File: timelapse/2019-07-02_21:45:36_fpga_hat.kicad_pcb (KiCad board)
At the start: 4 copper layers, 65 x 56.5 mm, 90 parts, among them J1 2x20, J2 AudioJack3, J3 Conn_02x06_Top_Bottom, J4 Conn_02x06_Top_Bottom, J5 Conn_02x06_Top_Bottom, J6 Conn_01x02, SW1 PTS815, SW2 PTS815, SW3 PTS815, SW4 PTS815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

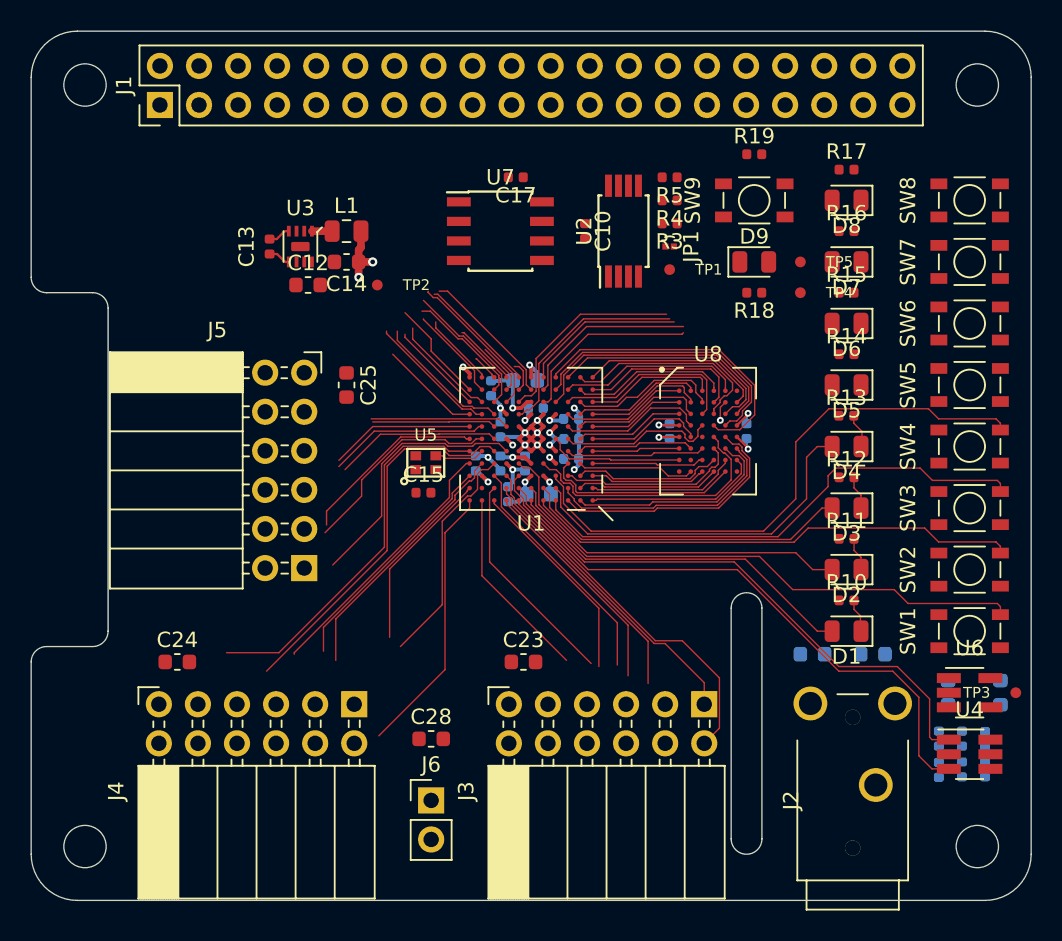
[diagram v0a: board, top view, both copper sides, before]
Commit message: Continue BGA route-out. SRAM connected, start heading out toward LEDs and IO.
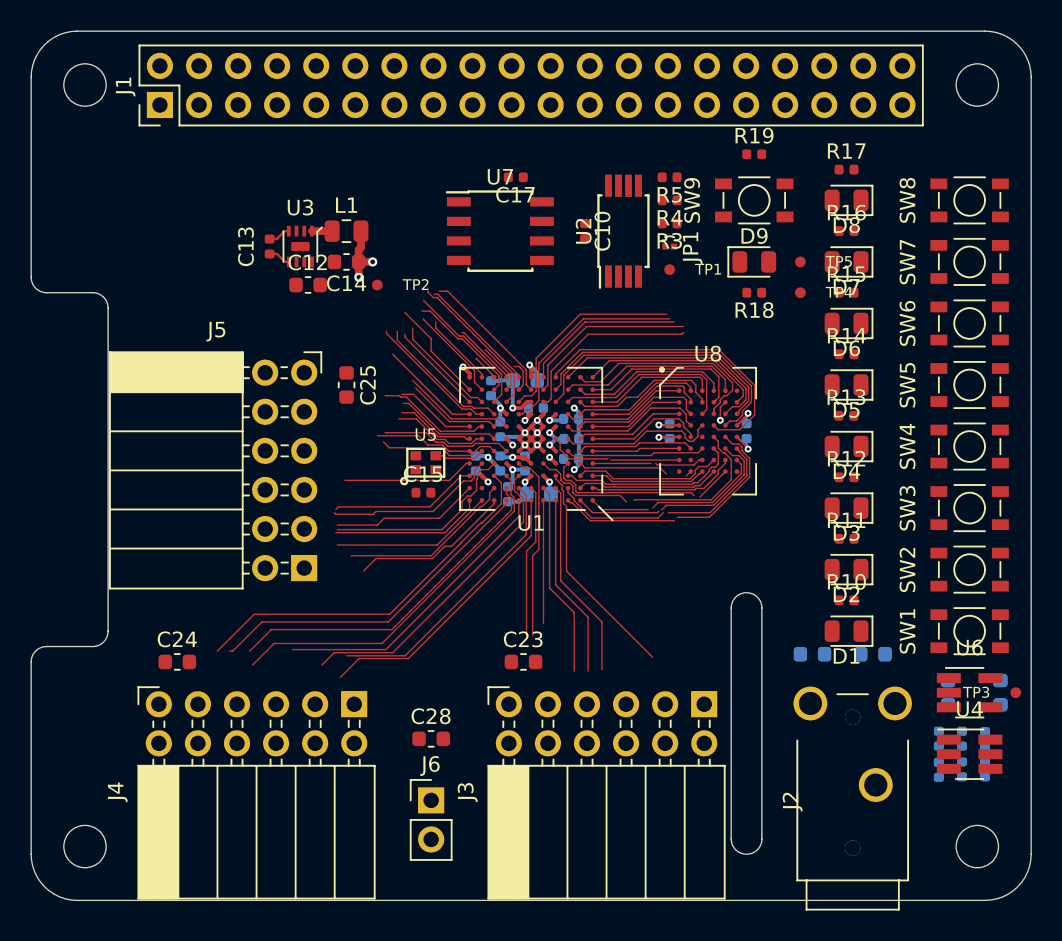
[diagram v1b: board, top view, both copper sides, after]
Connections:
- U1 pad A1: /SRAM_DQ7 -> /IO2_4
- U1 pad A11: /IO0_6 -> /IO0_0
- U1 pad A2: /SRAM_DQ5 -> /IO2_2
- U1 pad A3: /SRAM_DQ4 -> /IO2_3
- U1 pad A4: /SW2 -> /IO1_6
- U1 pad A5: /SW1 -> /IO1_4
- U1 pad A6: /LED0 -> /IO1_3
- U1 pad A7: /IO0_4 -> /IO1_2
- U1 pad B3: /SRAM_DQ6 -> /IO2_1
- U1 pad B4: /LED3 -> /IO2_0
- U1 pad B5: /LED2 -> /IO1_5
- U1 pad B6: /SW0 -> /IO2_6
- U1 pad B7: /AUDIO_L_PWM -> /IO2_5
- U1 pad B8: /IO1_2 -> /IO0_4
- U1 pad C4: /SW3 -> /SRAM_A11
- U1 pad C7: /AUDIO_R_PWM -> /IO1_1
- U1 pad C8: /IO0_0 -> /IO0_6
- U1 pad D2: /SRAM_A8 -> /SRAM_DQ15
- U1 pad D3: /SRAM_A11 -> /SRAM_A8
- U1 pad D5: /SRAM_A16 -> /IO1_7
- U1 pad D7: /LED1 -> /IO0_7
- U1 pad E8: /IO2_1 -> /SW3
- U1 pad E9: /IO1_6 -> /SW2
- U1 pad F10: /IO2_6 -> /SW0
- U1 pad F11: /IO2_5 -> /AUDIO_L_PWM
- U1 pad F4: /SRAM_DQ15 -> /SRAM_DQ6
- U1 pad F9: /IO1_4 -> /SW1
- U1 pad G8: /IO2_0 -> /LED3
- U1 pad H10: /IO0_7 -> /LED1
- U1 pad H7: /IO2_4 -> /SRAM_DQ7
- U1 pad J10: /IO1_5 -> /LED2
- U1 pad J5: /IO2_2 -> /SRAM_DQ5
- U1 pad J7: /IO2_3 -> /SRAM_DQ4
- U1 pad J8: /GP27_SDIO_DAT3 -> /GP22_SDIO_CLK
- U1 pad K11: /IO1_3 -> /LED0
- U1 pad K5: /IO1_7 -> /SRAM_A16
- U1 pad K6: /GP22_SDIO_CLK -> /GP27_SDIO_DAT3
- U1 pad K7: /IO1_1 -> /AUDIO_R_PWM
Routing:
- net /AUDIO_R_PWM: track 39.3 -> 2.04 mm
- net /AUDIO_L_PWM: track 36.5 -> 5.10 mm
- net /SW3: track 37.4 -> 8.55 mm
- net /SW0: track 34.7 -> 6.19 mm
- net /SW2: track 33.4 -> 7.96 mm
- net /SW1: track 32.3 -> 6.85 mm
- net /IO1_1: track 2.04 -> 20.4 mm
- net /SW5: track 24.6 -> 6.41 mm
- net /LED0: track 23.3 -> 6.74 mm
- net /LED3: track 23.7 -> 7.34 mm
- net /LED1: track 24.3 -> 8.53 mm
- net /LED2: track 21.5 -> 6.91 mm
- net /IO1_6: track 24.6 -> 12.0 mm
- net /IO1_3: track 6.74 -> 18.5 mm
- net /IO0_0: track 20.6 -> 9.86 mm
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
